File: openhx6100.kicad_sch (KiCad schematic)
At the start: 42 parts, among them J1 USB_C_Receptacle_PowerOnly_6P, Q1 DMG1012T, Q3 DMG1012T, Q5 DMG2301L, Q6 DMG2301L, Q7 DMG1012T, Q8 DMG1012T, U1 74HC14, U2 TLC555xD

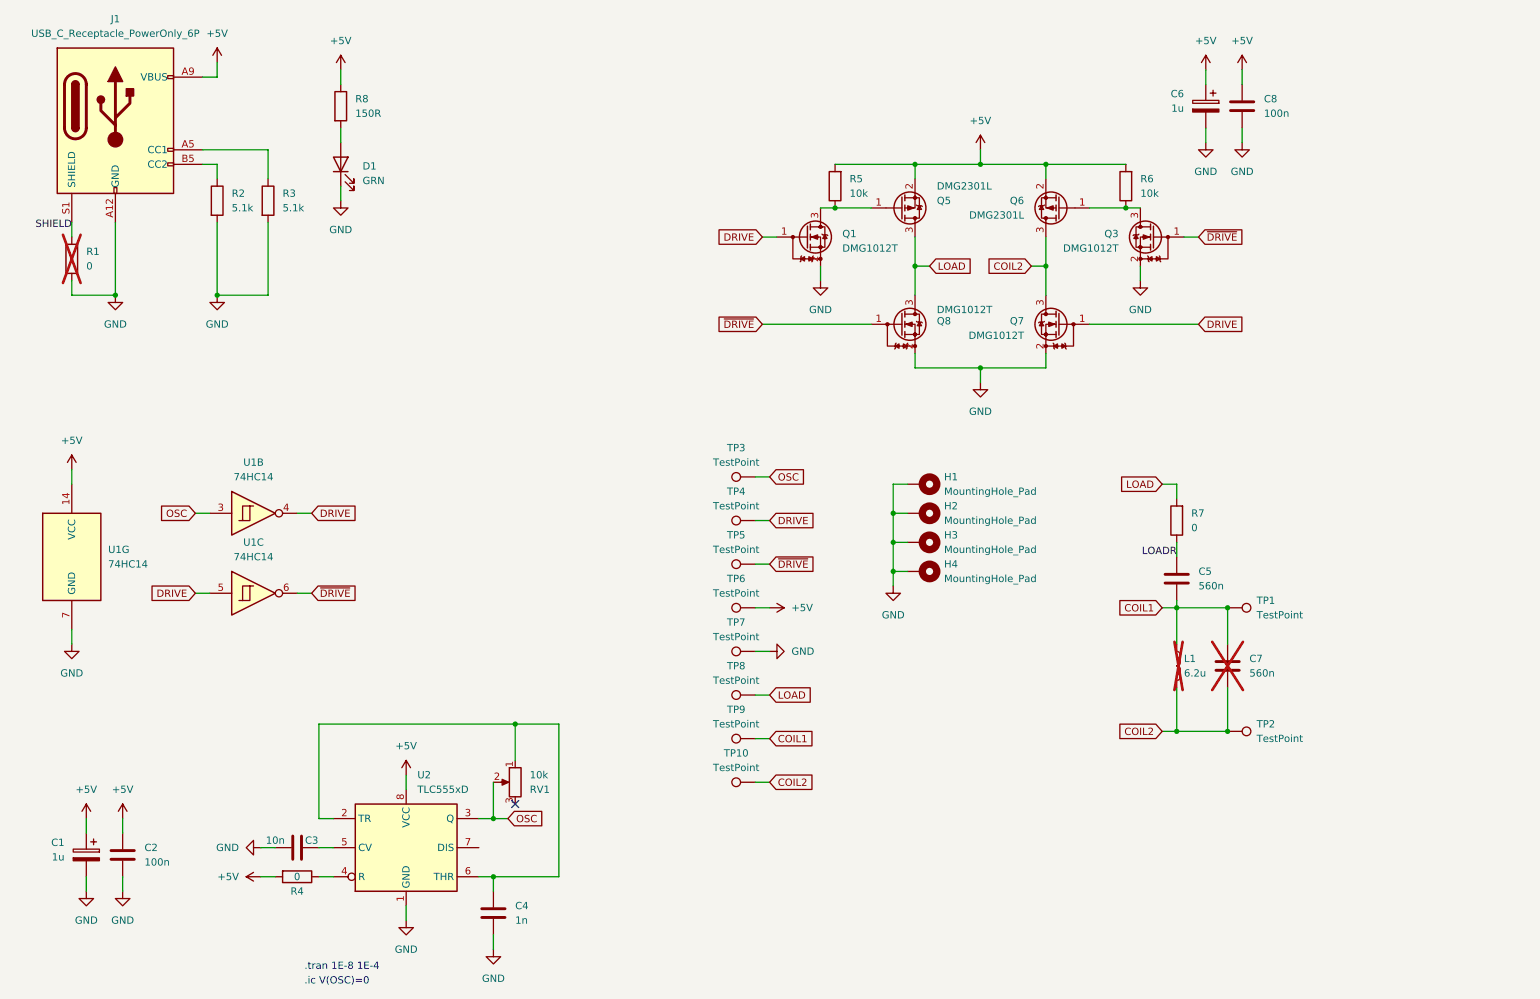
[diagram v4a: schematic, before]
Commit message: bom: fill out bom
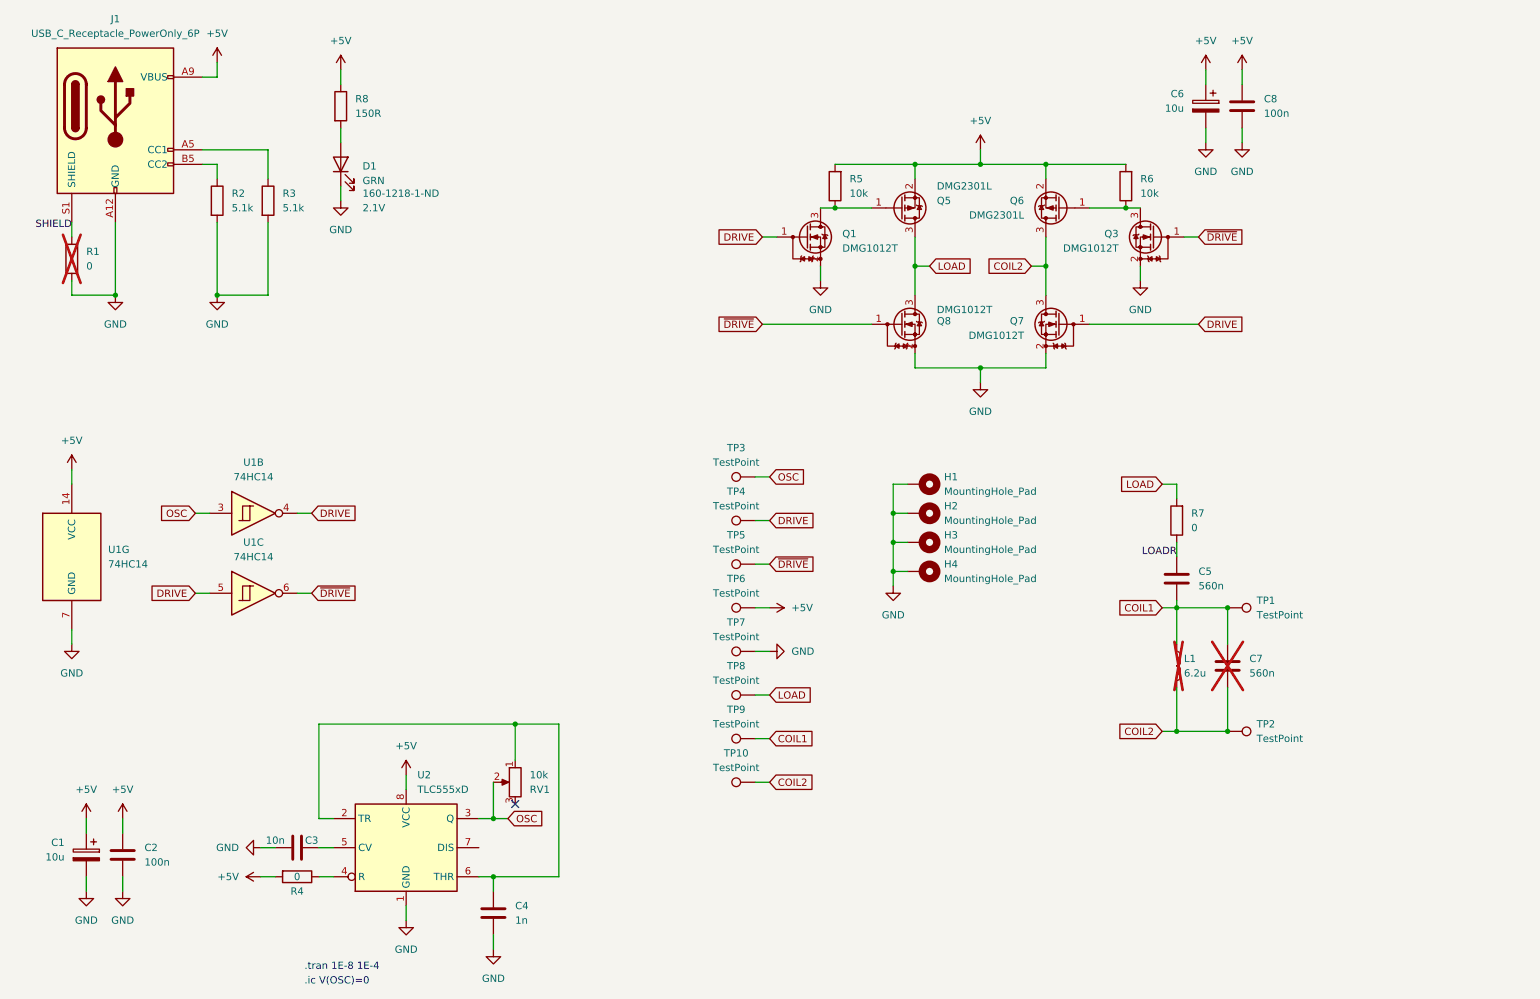
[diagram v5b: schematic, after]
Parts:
- C1, C6: value 1u -> 10u; footprint Capacitor_SMD:CP_Elec_4x4.5 -> Capacitor_SMD:CP_Elec_4x5.4; DigiKey Part Number 732-8851-1-ND -> (none); Digikey (none) -> 493-2173-1-ND
- C2, C8: DigiKey Part Number 399-4264-ND -> (none); Digikey (none) -> 478-KGM21NR71H104KMCT-ND
- C3: DigiKey Part Number K103K10X7RF53L2-ND -> (none); Digikey (none) -> CC0805KRX7R9BB103
- C4: DigiKey Part Number 445-173171-1-ND -> (none); Digikey (none) -> 399-C0805C102K5RAC7800CT-ND
- C5, C7: DigiKey Part Number 399-13965-ND -> (none); Digikey (none) -> 399-C0805C564K5RAC7800CT-ND
- D1: footprint LED_SMD:LED_0603_1608Metric_Pad1.05x0.95mm_HandSolder -> LED_SMD:LED_0805_2012Metric_Pad1.15x1.40mm_HandSolder; Digikey (none) -> 160-1218-1-ND; Vf (none) -> 2.1V
- J1: Digikey (none) -> 2223-UJC-HP-3-SMT-CT-ND
- L1: DigiKey Part Number 445-174580-ND -> (none); Digikey (none) -> 445-174580-ND
- Q1, Q3, Q7, Q8: Digikey (none) -> DMG1012T-7DICT-ND
- Q5, Q6: Digikey (none) -> DMG2301L-7DICT-ND
- R1, R4: Digikey (none) -> RMCF0805ZT0R00CT-ND
- R2, R3: Digikey (none) -> 311-5.1KARCT-ND
- R5, R6: DigiKey Part Number 13-MFR-25FRF52-10KCT-ND -> (none); Digikey (none) -> 311-10KARCT-ND
- R7: DigiKey Part Number 13-MFR-25FRF52-10KCT-ND -> (none); Digikey (none) -> RMCF0805ZT0R00CT-ND
- R8: Digikey (none) -> 311-150HRCT-ND
- RV1: Digikey (none) -> TC33X-103ECT-ND
- TP10, TP3, TP4, TP5, TP6, TP7, TP8, TP9: Digikey (none) -> 36-5000-ND
- U1: Digikey (none) -> 296-8234-1-ND
- U2: DigiKey Part Number 296-1857-5-ND -> (none); Digikey (none) -> 296-1336-1-ND

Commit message: feature: add revision info
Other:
- title: (none) -> openhx6100
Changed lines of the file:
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@@
 (kicad_sch (version 20230121) (generator eeschema)
   (paper "A4")
+  (title_block
+    (title "openhx6100")
+    (date "${DATE}")
+    (rev "${TAG} (${HASH})")
+  )
   (junction (at 175.26 46.99) (diameter 0) (color 0 0 0 0)
   )
